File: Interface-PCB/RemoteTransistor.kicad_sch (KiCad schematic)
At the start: 13 parts, among them IC2 TBD62783A, IC3 TBD62783A, J14 CONN_05JST, J15 CONN_05JST, U3 CD74HC4067_MUX

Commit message: Update schematic based on breadboard tests
- Add current limiting resistors to Level Shifter output
- Add pull down resistors on all Mux outputs
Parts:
- removed R12, R13, R14, R15, R16, R17: 10k, Resistor_THT:R_Axial_DIN0207_L6.3mm_D2.5mm_P10.16mm_Horizontal, symbol AA_Custom_Components:R
- added R12, R13, R14, R15, R16, R17, R18, R19, R20, R21, R22, R23, R24, R25, R26, R27: 10k, Resistor_THT:R_Axial_DIN0207_L6.3mm_D2.5mm_P10.16mm_Horizontal, symbol Device:R
- renumbered C9 to C2, C8 to C3
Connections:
- net GND: now also R12.2, R13.2, R14.2, R15.2, R16.2, R17.2, R18.2, R19.2, R20.2, R21.2, R22.2, R23.2, R24.2, R25.2, R26.2, R27.2
- net OUTLET_1_OFF: now also R21.1
- net OUTLET_1_ON: now also R26.1
- net OUTLET_2_OFF: now also R20.1
- net OUTLET_2_ON: now also R25.1
- net OUTLET_3_OFF: now also R19.1
- net OUTLET_3_ON: now also R24.1
- net OUTLET_4_OFF: now also R18.1
- net OUTLET_4_ON: now also R23.1
- net OUTLET_5_OFF: now also R17.1
- net OUTLET_5_ON: now also R22.1
- net at U3.1 (C15): now also R12.1
- net at U3.16 (C0): now also R27.1
- net at U3.2 (C14): now also R13.1
- net at U3.3 (C13): now also R14.1
- net at U3.4 (C12): now also R15.1
- net at U3.5 (C11): now also R16.1
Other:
- note added: "EN is active low. All outputs are disconnected when driven high. Use "Break-before-make""
- note added: "Note: Unused pins connected to GND through pulldown"
- note removed: "Note: Unused pins connected to GND through pulldown EN is active low. All outputs are disconnected when driven high. "Break-before-make""
- moved on the sheet: C2, C3, IC2, IC3, J14, J15, U3

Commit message: Add footprints for pads
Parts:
- R12, R13, R14, R15, R16, R17, R18, R19, R20, R21, R22, R23, R24, R25, R26, R27: footprint Resistor_THT:R_Axial_DIN0207_L6.3mm_D2.5mm_P10.16mm_Horizontal -> AA_Custom_Components:R_SS_Axial_DIN0207_L6.3mm_D2.5mm_P10.16mm_Horizontal
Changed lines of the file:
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@@
       (effects (font (size 1.27 1.27)) (justify left))
     )
-    (property "Footprint" "Resistor_THT:R_Axial_DIN0207_L6.3mm_D2.5mm_P10.16mm_Horizontal" (id 2) (at 70.612 68.58 90)
+    (property "Footprint" "AA_Custom_Components:R_SS_Axial_DIN0207_L6.3mm_D2.5mm_P10.16mm_Horizontal" (id 2) (at 70.612 68.58 90)
       (effects (font (size 1.27 1.27)) hide)
     )
@@
       (effects (font (size 1.27 1.27)) (justify left))
     )
-    (property "Footprint" "Resistor_THT:R_Axial_DIN0207_L6.3mm_D2.5mm_P10.16mm_Horizontal" (id 2) (at 131.572 68.58 90)
+    (property "Footprint" "AA_Custom_Components:R_SS_Axial_DIN0207_L6.3mm_D2.5mm_P10.16mm_Horizontal" (id 2) (at 131.572 68.58 90)
       (effects (font (size 1.27 1.27)) hide)
     )
@@
       (effects (font (size 1.27 1.27)) (justify left))
     )
-    (property "Footprint" "Resistor_THT:R_Axial_DIN0207_L6.3mm_D2.5mm_P10.16mm_Horizontal" (id 2) (at 78.232 68.58 90)
+    (property "Footprint" "AA_Custom_Components:R_SS_Axial_DIN0207_L6.3mm_D2.5mm_P10.16mm_Horizontal" (id 2) (at 78.232 68.58 90)
       (effects (font (size 1.27 1.27)) hide)
     )
@@
       (effects (font (size 1.27 1.27)) (justify left))
     )
-    (property "Footprint" "Resistor_THT:R_Axial_DIN0207_L6.3mm_D2.5mm_P10.16mm_Horizontal" (id 2) (at 139.192 68.58 90)
+    (property "Footprint" "AA_Custom_Components:R_SS_Axial_DIN0207_L6.3mm_D2.5mm_P10.16mm_Horizontal" (id 2) (at 139.192 68.58 90)
       (effects (font (size 1.27 1.27)) hide)
     )
@@
       (effects (font (size 1.27 1.27)) (justify left))
     )
-    (property "Footprint" "Resistor_THT:R_Axial_DIN0207_L6.3mm_D2.5mm_P10.16mm_Horizontal" (id 2) (at 62.992 68.58 90)
+    (property "Footprint" "AA_Custom_Components:R_SS_Axial_DIN0207_L6.3mm_D2.5mm_P10.16mm_Horizontal" (id 2) (at 62.992 68.58 90)
       (effects (font (size 1.27 1.27)) hide)
     )
@@
       (effects (font (size 1.27 1.27)) (justify left))
     )
-    (property "Footprint" "Resistor_THT:R_Axial_DIN0207_L6.3mm_D2.5mm_P10.16mm_Horizontal" (id 2) (at 85.852 68.58 90)
+    (property "Footprint" "AA_Custom_Components:R_SS_Axial_DIN0207_L6.3mm_D2.5mm_P10.16mm_Horizontal" (id 2) (at 85.852 68.58 90)
       (effects (font (size 1.27 1.27)) hide)
     )
@@
       (effects (font (size 1.27 1.27)) (justify left))
     )
-    (property "Footprint" "Resistor_THT:R_Axial_DIN0207_L6.3mm_D2.5mm_P10.16mm_Horizontal" (id 2) (at 47.752 68.58 90)
+    (property "Footprint" "AA_Custom_Components:R_SS_Axial_DIN0207_L6.3mm_D2.5mm_P10.16mm_Horizontal" (id 2) (at 47.752 68.58 90)
       (effects (font (size 1.27 1.27)) hide)
     )
@@
       (effects (font (size 1.27 1.27)) (justify left))
     )
-    (property "Footprint" "Resistor_THT:R_Axial_DIN0207_L6.3mm_D2.5mm_P10.16mm_Horizontal" (id 2) (at 101.092 68.58 90)
+    (property "Footprint" "AA_Custom_Components:R_SS_Axial_DIN0207_L6.3mm_D2.5mm_P10.16mm_Horizontal" (id 2) (at 101.092 68.58 90)
       (effects (font (size 1.27 1.27)) hide)
     )
@@
       (effects (font (size 1.27 1.27)) (justify left))
     )
-    (property "Footprint" "Resistor_THT:R_Axial_DIN0207_L6.3mm_D2.5mm_P10.16mm_Horizontal" (id 2) (at 40.132 68.58 90)
+    (property "Footprint" "AA_Custom_Components:R_SS_Axial_DIN0207_L6.3mm_D2.5mm_P10.16mm_Horizontal" (id 2) (at 40.132 68.58 90)
       (effects (font (size 1.27 1.27)) hide)
     )
@@
       (effects (font (size 1.27 1.27)) (justify left))
     )
-    (property "Footprint" "Resistor_THT:R_Axial_DIN0207_L6.3mm_D2.5mm_P10.16mm_Horizontal" (id 2) (at 154.432 68.58 90)
+    (property "Footprint" "AA_Custom_Components:R_SS_Axial_DIN0207_L6.3mm_D2.5mm_P10.16mm_Horizontal" (id 2) (at 154.432 68.58 90)
       (effects (font (size 1.27 1.27)) hide)
     )
@@
       (effects (font (size 1.27 1.27)) (justify left))
     )
-    (property "Footprint" "Resistor_THT:R_Axial_DIN0207_L6.3mm_D2.5mm_P10.16mm_Horizontal" (id 2) (at 93.472 68.58 90)
+    (property "Footprint" "AA_Custom_Components:R_SS_Axial_DIN0207_L6.3mm_D2.5mm_P10.16mm_Horizontal" (id 2) (at 93.472 68.58 90)
       (effects (font (size 1.27 1.27)) hide)
     )
@@
       (effects (font (size 1.27 1.27)) (justify left))
     )
-    (property "Footprint" "Resistor_THT:R_Axial_DIN0207_L6.3mm_D2.5mm_P10.16mm_Horizontal" (id 2) (at 146.812 68.58 90)
+    (property "Footprint" "AA_Custom_Components:R_SS_Axial_DIN0207_L6.3mm_D2.5mm_P10.16mm_Horizontal" (id 2) (at 146.812 68.58 90)
       (effects (font (size 1.27 1.27)) hide)
     )
@@
       (effects (font (size 1.27 1.27)) (justify left))
     )
-    (property "Footprint" "Resistor_THT:R_Axial_DIN0207_L6.3mm_D2.5mm_P10.16mm_Horizontal" (id 2) (at 55.372 68.58 90)
+    (property "Footprint" "AA_Custom_Components:R_SS_Axial_DIN0207_L6.3mm_D2.5mm_P10.16mm_Horizontal" (id 2) (at 55.372 68.58 90)
       (effects (font (size 1.27 1.27)) hide)
     )
@@
       (effects (font (size 1.27 1.27)) (justify left))
     )
-    (property "Footprint" "Resistor_THT:R_Axial_DIN0207_L6.3mm_D2.5mm_P10.16mm_Horizontal" (id 2) (at 123.952 68.58 90)
+    (property "Footprint" "AA_Custom_Components:R_SS_Axial_DIN0207_L6.3mm_D2.5mm_P10.16mm_Horizontal" (id 2) (at 123.952 68.58 90)
       (effects (font (size 1.27 1.27)) hide)
     )
@@
       (effects (font (size 1.27 1.27)) (justify left))
     )
-    (property "Footprint" "Resistor_THT:R_Axial_DIN0207_L6.3mm_D2.5mm_P10.16mm_Horizontal" (id 2) (at 108.712 68.58 90)
+    (property "Footprint" "AA_Custom_Components:R_SS_Axial_DIN0207_L6.3mm_D2.5mm_P10.16mm_Horizontal" (id 2) (at 108.712 68.58 90)
       (effects (font (size 1.27 1.27)) hide)
     )
@@
       (effects (font (size 1.27 1.27)) (justify left))
     )
-    (property "Footprint" "Resistor_THT:R_Axial_DIN0207_L6.3mm_D2.5mm_P10.16mm_Horizontal" (id 2) (at 116.332 68.58 90)
-      (effects (font (size 1.27 1.27)) hide)
-    )
+    (property "Footprint" "AA_Custom_Components:R_SS_Axial_DIN0207_L6.3mm_D2.5mm_P10.16mm_Horizontal" (id 2) (at 116.332 68.58 90)
+      (effects (font (size 1.27 1.27)) hide)
+    )

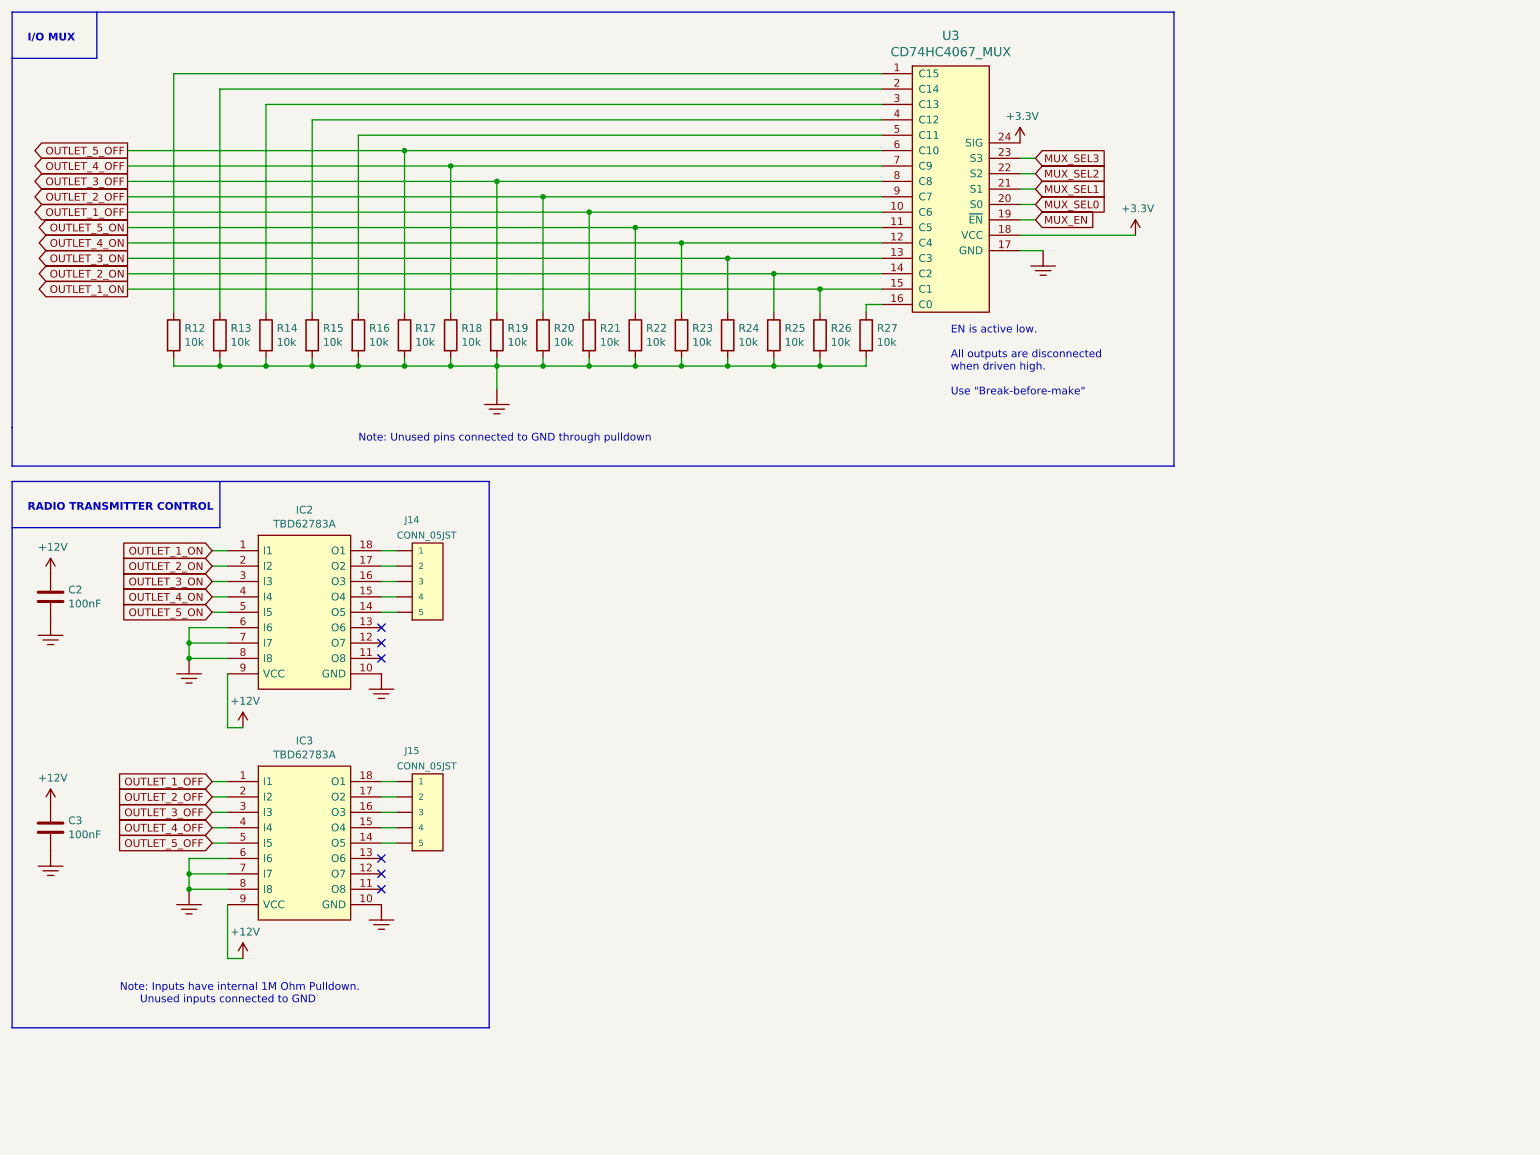
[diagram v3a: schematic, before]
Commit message: Add breakout board and IC footprints
- MUX
- Motor Driver
- PDIP ICs
- LEDs
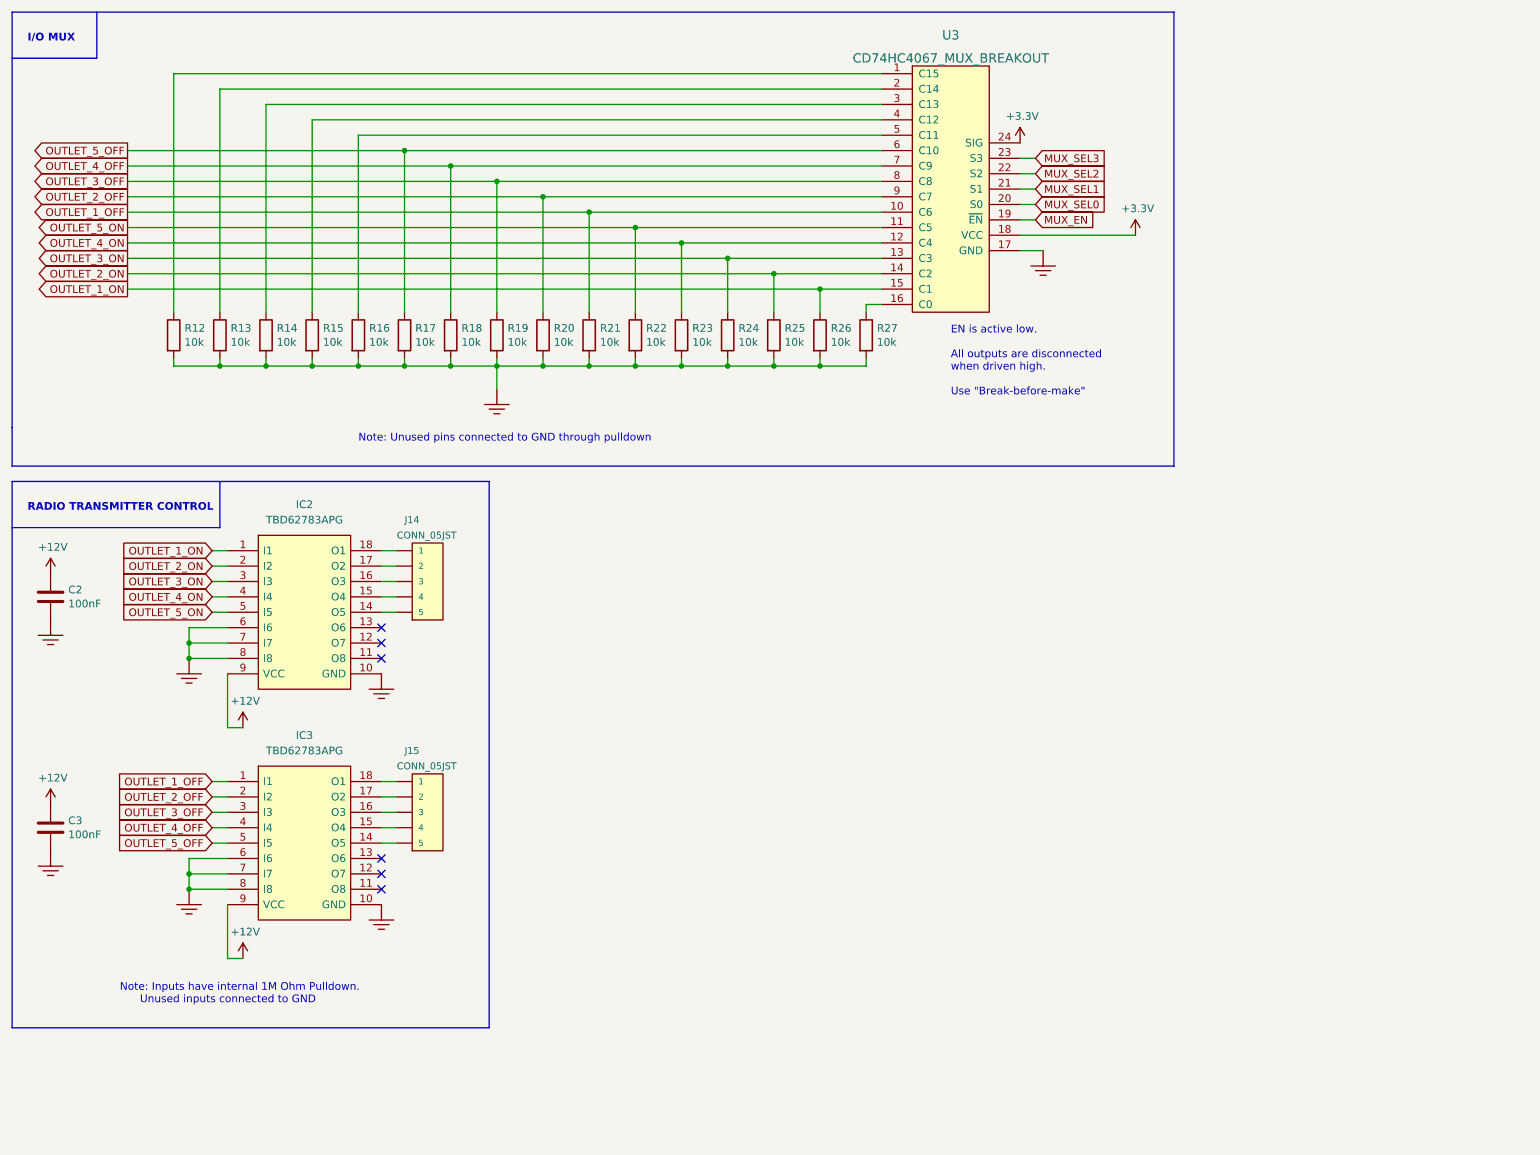
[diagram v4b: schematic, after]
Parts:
- removed IC2, IC3: TBD62783A, Package_DIP:DIP-18_W7.62mm_LongPads, symbol AA_Custom_Components:TBD62783A
- removed U3: CD74HC4067_MUX, digikey-footprints:Socket_DIP-24_15.24mm_Conn, symbol AA_Custom_Components:CD74HC4067_MUX
- added IC2, IC3: TBD62783APG, AA_Custom_Components:DIP-18_W7.62mm_Socket_IC, symbol AA_Custom_Components:TBD62783APG
- added U3: CD74HC4067_MUX_BREAKOUT, AA_Custom_Components:CD74HC4067_MUX_BREAKOUT, symbol AA_Custom_Components:CD74HC4067_MUX_BREAKOUT
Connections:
- net +12V: now also IC2.9 (VCC), IC3.9 (VCC)
- net +3V3: now also U3.18 (VCC), U3.24 (SIG)
- net GND: now also IC2.10 (GND), IC2.6 (I6), IC2.7 (I7), IC2.8 (I8), IC3.10 (GND), IC3.6 (I6), IC3.7 (I7), IC3.8 (I8), U3.17 (GND)
- net MUX_EN: now also U3.19 (~{EN})
- net MUX_SEL0: now also U3.20 (S0)
- net MUX_SEL1: now also U3.21 (S1)
- net MUX_SEL2: now also U3.22 (S2)
- net MUX_SEL3: now also U3.23 (S3)
- net OUTLET_1_OFF: now also IC3.1 (I1), U3.10 (C6)
- net OUTLET_1_ON: now also IC2.1 (I1), U3.15 (C1)
- net OUTLET_2_OFF: now also IC3.2 (I2), U3.9 (C7)
- net OUTLET_2_ON: now also IC2.2 (I2), U3.14 (C2)
- net OUTLET_3_OFF: now also IC3.3 (I3), U3.8 (C8)
- net OUTLET_3_ON: now also IC2.3 (I3), U3.13 (C3)
- net OUTLET_4_OFF: now also IC3.4 (I4), U3.7 (C9)
- net OUTLET_4_ON: now also IC2.4 (I4), U3.12 (C4)
- net OUTLET_5_OFF: now also IC3.5 (I5), U3.6 (C10)
- net OUTLET_5_ON: now also IC2.5 (I5), U3.11 (C5)
- net at J14.1: now also IC2.18 (O1)
- net at J14.2: now also IC2.17 (O2)
- net at J14.3: now also IC2.16 (O3)
- net at J14.4: now also IC2.15 (O4)
- net at J14.5: now also IC2.14 (O5)
- net at J15.1: now also IC3.18 (O1)
- net at J15.2: now also IC3.17 (O2)
- net at J15.3: now also IC3.16 (O3)
- net at J15.4: now also IC3.15 (O4)
- net at J15.5: now also IC3.14 (O5)
- net at R12.1: now also U3.1 (C15)
- net at R27.1: now also U3.16 (C0)
- net at R13.1: now also U3.2 (C14)
- net at R14.1: now also U3.3 (C13)
- net at R15.1: now also U3.4 (C12)
- net at R16.1: now also U3.5 (C11)

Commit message: Add JST Connector Footprints
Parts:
- C2, C3: footprint Capacitor_THT:C_Disc_D3.4mm_W2.1mm_P2.50mm -> AA_Custom_Components:C_Ceramic_Disc_D4.3mm_W1.9mm_P5.08mm
- J14, J15: footprint Connector_JST:JST_XH_B5B-XH-A_1x05_P2.50mm_Vertical -> AA_Custom_Components:JST_XH_1x05_P2.54mm_Vertical
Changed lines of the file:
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@@
       (effects (font (size 1.143 1.143)) (justify right))
     )
-    (property "Footprint" "Connector_JST:JST_XH_B5B-XH-A_1x05_P2.50mm_Vertical" (id 2) (at 81.28 99.06 0)
+    (property "Footprint" "AA_Custom_Components:JST_XH_1x05_P2.54mm_Vertical" (id 2) (at 81.28 99.06 0)
       (effects (font (size 0.508 0.508)) hide)
     )
@@
       (effects (font (size 1.143 1.143)) (justify right))
     )
-    (property "Footprint" "Connector_JST:JST_XH_B5B-XH-A_1x05_P2.50mm_Vertical" (id 2) (at 81.28 137.16 0)
+    (property "Footprint" "AA_Custom_Components:JST_XH_1x05_P2.54mm_Vertical" (id 2) (at 81.28 137.16 0)
       (effects (font (size 0.508 0.508)) hide)
     )
@@
       (effects (font (size 1.27 1.27)) (justify left))
     )
-    (property "Footprint" "Capacitor_THT:C_Disc_D3.4mm_W2.1mm_P2.50mm" (id 2) (at 22.5552 115.57 0)
+    (property "Footprint" "AA_Custom_Components:C_Ceramic_Disc_D4.3mm_W1.9mm_P5.08mm" (id 2) (at 22.5552 115.57 0)
       (effects (font (size 1.27 1.27)) hide)
     )
@@
       (effects (font (size 1.27 1.27)) (justify left))
     )
-    (property "Footprint" "Capacitor_THT:C_Disc_D3.4mm_W2.1mm_P2.50mm" (id 2) (at 22.5552 153.67 0)
+    (property "Footprint" "AA_Custom_Components:C_Ceramic_Disc_D4.3mm_W1.9mm_P5.08mm" (id 2) (at 22.5552 153.67 0)
       (effects (font (size 1.27 1.27)) hide)
     )
